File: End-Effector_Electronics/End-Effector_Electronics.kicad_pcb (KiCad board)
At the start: 2 copper layers, 65 x 57 mm, 34 parts, among them J1 Raspberry_Pi_2_3, J2 LynxServo, J3 LynxServo, J4 QWIIC_Generic_Conn, Q1 Q_PMOS_GSD, Q2 DMMT3906, Q3 Q_NMOS_GSD, U1 CAT24C32, U2 TDK_I3A4W008A033V, U3 LM22676MR-5

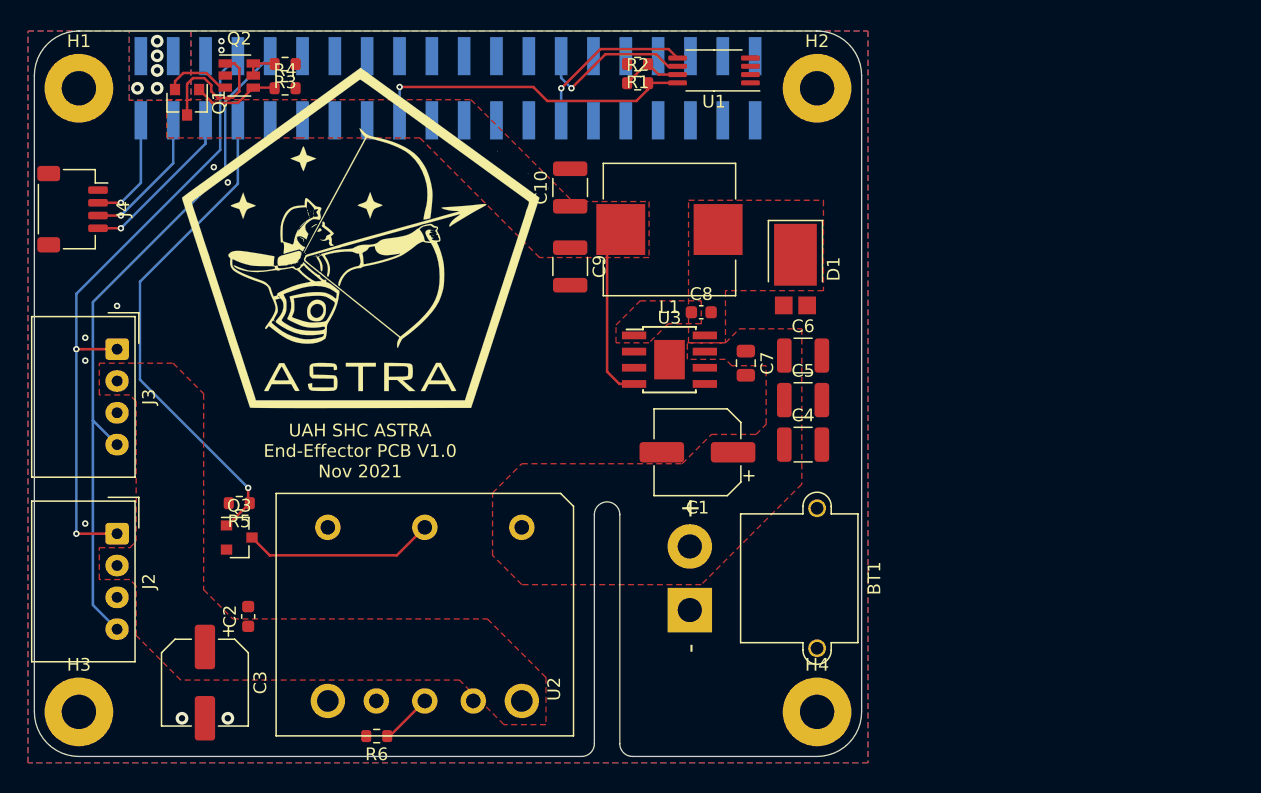
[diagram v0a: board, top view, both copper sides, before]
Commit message: added things and cleaned up silkscreen
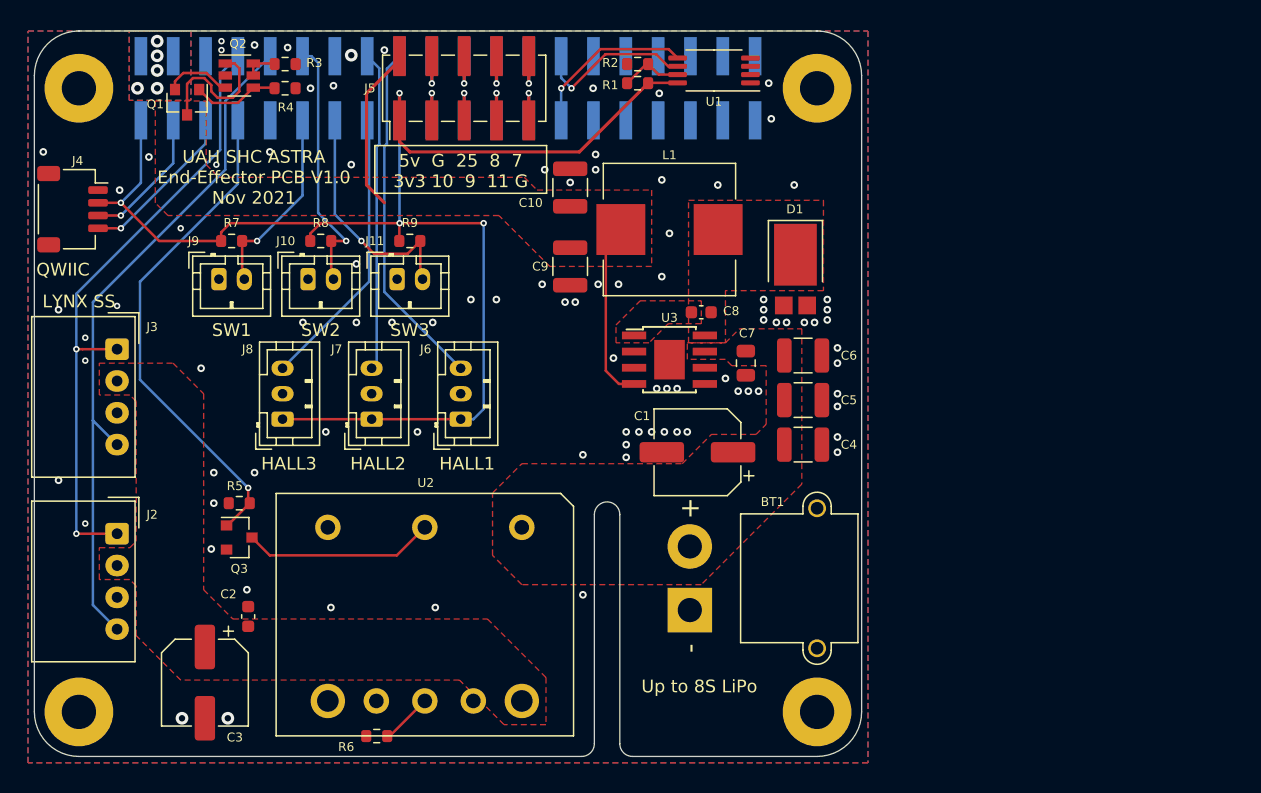
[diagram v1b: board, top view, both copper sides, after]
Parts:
- added J10: SW_Push_Open, Connector_JST:JST_PH_B2B-PH-K_1x02_P2.00mm_Vertical, F.Cu at (184.6, 97.5)
- added J11: SW_Push_Open, Connector_JST:JST_PH_B2B-PH-K_1x02_P2.00mm_Vertical, F.Cu at (191.6, 97.5)
- added J5: Conn_02x05_Odd_Even, Connector_PinHeader_2.54mm:PinHeader_2x05_P2.54mm_Vertical_SMD, F.Cu at (196.8, 82.5)
- added J6: AH1815-P-B, Connector_JST:JST_PH_B3B-PH-K_1x03_P2.00mm_Vertical, F.Cu at (196.6, 108.5)
- added J7: AH1815-P-B, Connector_JST:JST_PH_B3B-PH-K_1x03_P2.00mm_Vertical, F.Cu at (189.6, 108.5)
- added J8: AH1815-P-B, Connector_JST:JST_PH_B3B-PH-K_1x03_P2.00mm_Vertical, F.Cu at (182.6, 108.5)
- added J9: SW_Push_Open, Connector_JST:JST_PH_B2B-PH-K_1x02_P2.00mm_Vertical, F.Cu at (177.6, 97.5)
- added R7: 100k, Resistor_SMD:R_0603_1608Metric, F.Cu at (178.6, 94.5)
- added R8: 100k, Resistor_SMD:R_0603_1608Metric, F.Cu at (185.6, 94.5)
- added R9: 100k, Resistor_SMD:R_0603_1608Metric, F.Cu at (192.6, 94.5)
- G***: moved to B.Cu
- moved G*** 25.2 mm to (212.9, 101.0), turned to 180 degrees
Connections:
- H1 pad 1: (no net) -> Net-(H1-Pad1)
- H2 pad 1: (no net) -> Net-(H2-Pad1)
- H3 pad 1: (no net) -> Net-(H3-Pad1)
- H4 pad 1: (no net) -> Net-(H4-Pad1)
- J1 pad 11: (no net) -> /Limit_SW1
- J1 pad 12: (no net) -> /Limit_SW2
- J1 pad 13: (no net) -> /Limit_SW3
- J1 pad 15: (no net) -> /Hall3
- J1 pad 16: (no net) -> /Hall2
- J1 pad 18: (no net) -> /Hall1
- J1 pad 19: (no net) -> /GPIO10
- J1 pad 21: (no net) -> /GPIO9
- J1 pad 22: (no net) -> /GPIO25
- J1 pad 23: (no net) -> /GPIO11
- J1 pad 24: (no net) -> /GPIO8
- J1 pad 26: (no net) -> /GPIO7
- J1 pad 29: (no net) -> Net-(J1-Pad29)
- J1 pad 31: (no net) -> Net-(J1-Pad31)
- J1 pad 32: (no net) -> /GPIO12
- J1 pad 33: (no net) -> /GPIO13
- J1 pad 35: (no net) -> Net-(J1-Pad35)
- J1 pad 36: (no net) -> Net-(J1-Pad36)
- J1 pad 37: (no net) -> Net-(J1-Pad37)
- J1 pad 38: (no net) -> Net-(J1-Pad38)
- J1 pad 40: (no net) -> Net-(J1-Pad40)
- U2 pad 3: (no net) -> Net-(U2-Pad3)
- U2 pad 5: (no net) -> Net-(U2-Pad5)
- U2 pad 7: (no net) -> Net-(U2-Pad7)
- U3 pad 2: (no net) -> Net-(U3-Pad2)
- U3 pad 3: (no net) -> Net-(U3-Pad3)
- U3 pad 5: (no net) -> Net-(U3-Pad5)
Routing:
- net +3V3: track 34.7 -> 112.0 mm, vias 2 -> 4
- net /Hall1: track 0.00 -> 27.5 mm
- net /Hall2: track 0.00 -> 25.2 mm
- net /Hall3: track 0.00 -> 22.4 mm
- net /Limit_SW2: track 0.00 -> 20.6 mm, vias 0 -> 1
- net /Limit_SW3: track 0.00 -> 18.9 mm, vias 0 -> 1
- net /Limit_SW1: track 0.00 -> 15.2 mm, vias 0 -> 1
- net +5V: track 25.1 -> 38.4 mm
- net GND: track 0.00 -> 8.57 mm, vias 10 -> 94
- net /GPIO9: track 0.00 -> 4.28 mm, vias 0 -> 1
- net /GPIO11: track 0.00 -> 4.28 mm, vias 0 -> 1
- net /GPIO10: track 0.00 -> 4.28 mm, vias 0 -> 1
- net /GPIO8: track 0.00 -> 4.28 mm, vias 0 -> 1
- net /GPIO7: track 0.00 -> 4.28 mm, vias 0 -> 1
- net /GPIO25: track 0.00 -> 4.28 mm, vias 0 -> 1
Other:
- board text added: "5v G 25 8 7 3v3 10 9 11 G"
- board text added: "HALL1"
- board text added: "HALL2"
- board text added: "HALL3"
- board text added: "LYNX SS"
- board text added: "QWIIC"
- board text added: "SW1"
- board text added: "SW2"
- board text added: "SW3"
- board text added: "Up to 8S LiPo"

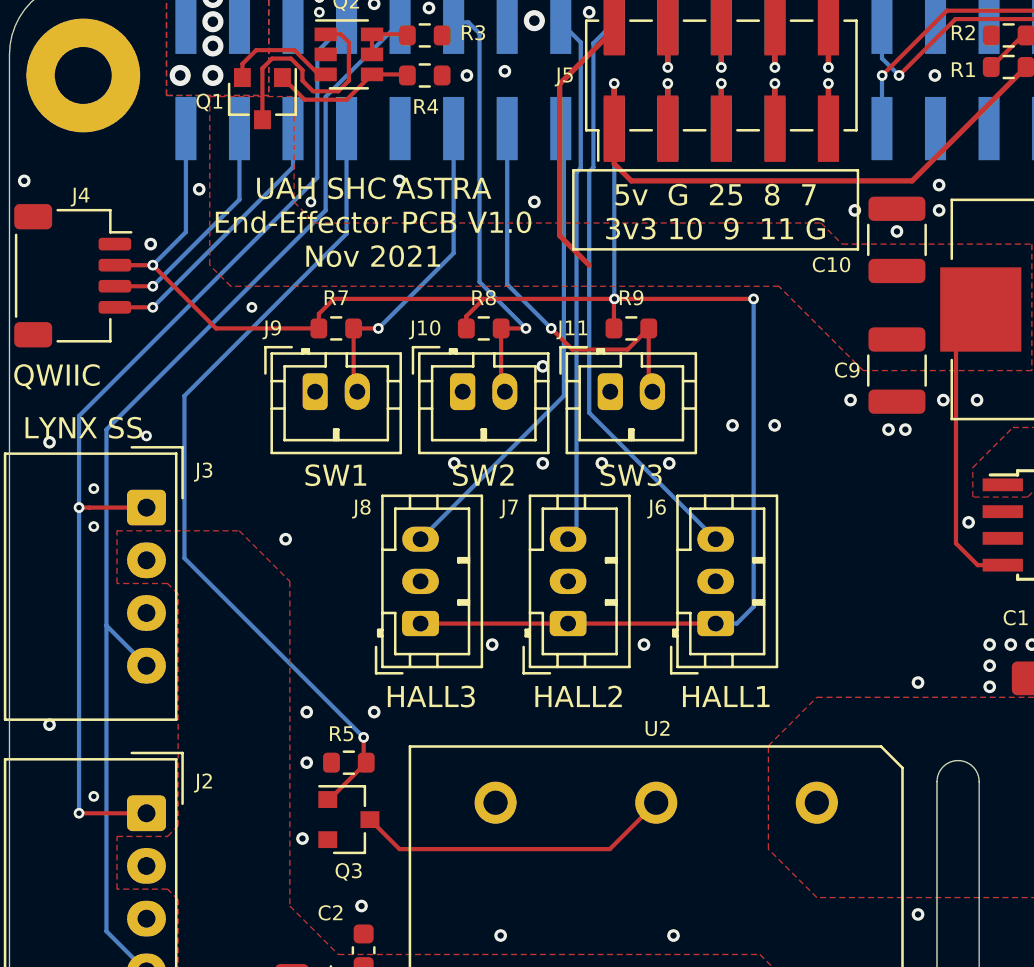
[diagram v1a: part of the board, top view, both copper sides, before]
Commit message: Swapped a few components
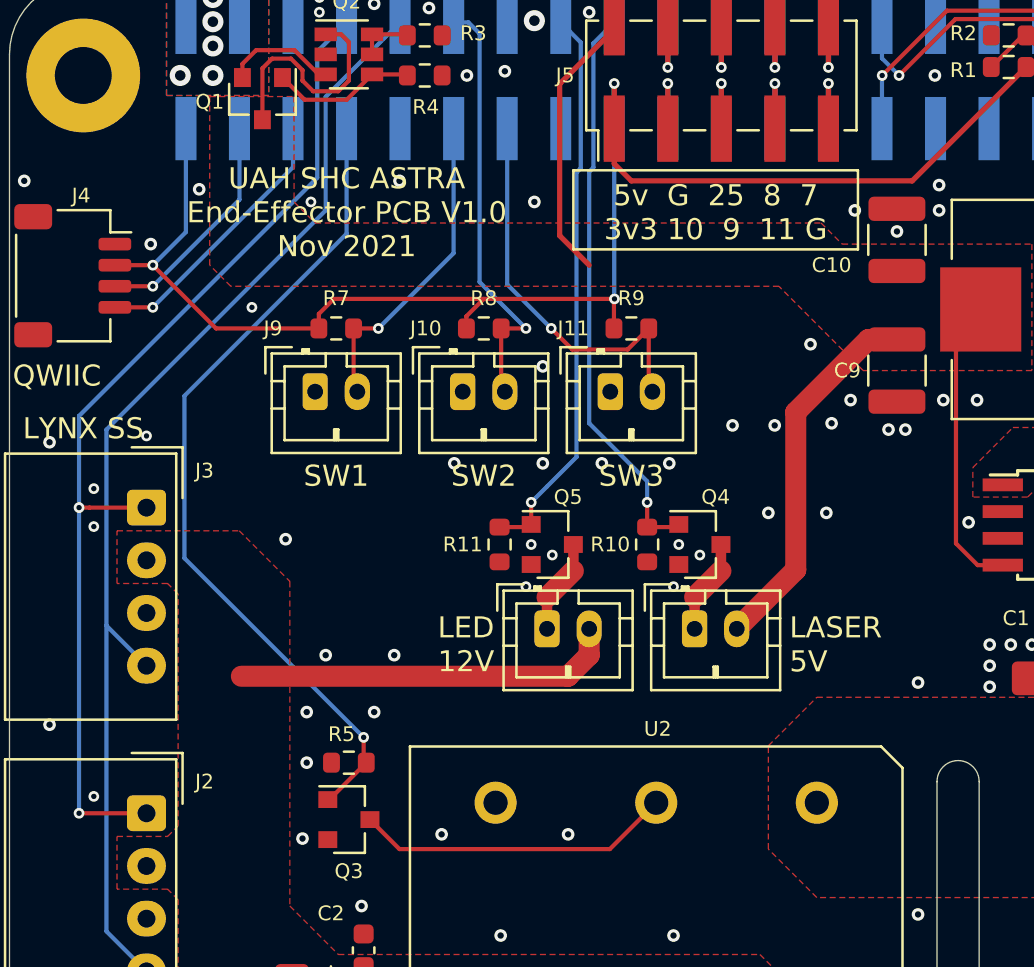
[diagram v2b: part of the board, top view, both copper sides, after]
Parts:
- removed J6, J7, J8: AH1815-P-B, Connector_JST:JST_PH_B3B-PH-K_1x03_P2.00mm_Vertical
- added D2: LED, Connector_JST:JST_PH_B2B-PH-K_1x02_P2.00mm_Vertical, F.Cu at (188.6, 108.8)
- added G***: LOGO, ASTRA_Footprints:SHCLogoSmall, B.Cu at (179.3, 109.0)
- added LD1: Laserdiode_1C2A, Connector_JST:JST_PH_B2B-PH-K_1x02_P2.00mm_Vertical, F.Cu at (195.6, 108.8)
- added Q4: Q_NMOS_GSD, Package_TO_SOT_SMD:SOT-23, F.Cu at (195.8, 104.8)
- added Q5: Q_NMOS_GSD, Package_TO_SOT_SMD:SOT-23, F.Cu at (188.8, 104.8)
- added R10: 100k, Resistor_SMD:R_0603_1608Metric, F.Cu at (193.3, 104.8)
- added R11: 100k, Resistor_SMD:R_0603_1608Metric, F.Cu at (186.3, 104.8)
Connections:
- J1 pad 15: /Hall3 -> Net-(J1-Pad15)
- J1 pad 16: /Hall2 -> /LED
- J1 pad 18: /Hall1 -> /Laser
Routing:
- net +3V3: track 112.0 -> 74.7 mm, vias 4 -> 3
- net /Hall1: track 27.5 -> 0.00 mm
- net /Laser: track 0.00 -> 27.1 mm, vias 0 -> 1
- net /LED: track 0.00 -> 26.7 mm, vias 0 -> 1
- net /Hall2: track 25.2 -> 0.00 mm
- net /Hall3: track 22.4 -> 0.00 mm
- net +12V: track 0.00 -> 18.2 mm
- net +5V: track 38.4 -> 56.0 mm
- net Net-(LD1-Pad1): track 0.00 -> 4.52 mm
- net Net-(D2-Pad1): track 0.00 -> 4.52 mm
- net GND: vias 94 -> 106
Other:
- board text added: "LASER 5V"
- board text added: "LED 12V"
- board text removed: "HALL1"
- board text removed: "HALL2"
- board text removed: "HALL3"

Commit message: tweaks
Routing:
- net GND: vias 106 -> 108
- net +BATT: vias 0 -> 8
- added copper zone on B.Cu, net +BATT
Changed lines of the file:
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@@
     (thickness 1.6)
     (drawings 28)
-    (tracks 304)
+    (tracks 314)
     (zones 0)
     (modules 48)
@@
   (gr_arc (start 166.58 131.55) (end 163.08 131.55) (angle -90) (layer Edge.Cuts) (width 0.05))
   (gr_arc (start 166.58 81.55) (end 166.58 78.05) (angle -90) (layer Edge.Cuts) (width 0.05))
+  (via (at 213.88 112.85) (size 0.6) (drill 0.3) (layers F.Cu B.Cu) (net 1))
+  (via (at 217.28 116.35) (size 0.6) (drill 0.3) (layers F.Cu B.Cu) (net 1))
+  (via (at 217.28 118.75) (size 0.6) (drill 0.3) (layers F.Cu B.Cu) (net 1))
+  (via (at 201.68 112.85) (size 0.6) (drill 0.3) (layers F.Cu B.Cu) (net 1))
+  (via (at 199.88 114.75) (size 0.6) (drill 0.3) (layers F.Cu B.Cu) (net 1))
+  (via (at 201.68 120.85) (size 0.6) (drill 0.3) (layers F.Cu B.Cu) (net 1))
+  (via (at 206.18 120.85) (size 0.6) (drill 0.3) (layers F.Cu B.Cu) (net 1))
+  (via (at 209.98 120.85) (size 0.6) (drill 0.3) (layers F.Cu B.Cu) (net 1))
   (via (at 178.28 132.05) (size 1) (drill 0.5) (layers F.Cu B.Cu) (net 2))
   (via (at 174.68 132.05) (size 1) (drill 0.5) (layers F.Cu B.Cu) (net 2))
@@
   (via (at 201.08 95.3) (size 0.6) (drill 0.3) (layers F.Cu B.Cu) (net 2))
   (via (at 202.08 99.05) (size 0.6) (drill 0.3) (layers F.Cu B.Cu) (net 2))
+  (via (at 213.08 101.65) (size 0.6) (drill 0.3) (layers F.Cu B.Cu) (net 2))
+  (via (at 213.88 101.65) (size 0.6) (drill 0.3) (layers F.Cu B.Cu) (net 2))
   (segment (start 189.58 111.05) (end 174.08 111.05) (width 1) (layer F.Cu) (net 3))
   (segment (start 190.58 110.05) (end 189.58 111.05) (width 1) (layer F.Cu) (net 3))
@@
       )
     )
+  )
+  (zone (net 1) (net_name +BATT) (layer B.Cu) (hatch edge 0.508)
+    (priority 9)
+    (connect_pads (clearance 0.2))
+    (min_thickness 0.2)
+    (fill yes (arc_segments 32) (thermal_gap 0.2) (thermal_bridge_width 1))
+    (polygon
+      (pts
+        (xy 215.48 121.55) (xy 201.38 121.55) (xy 199.08 119.25) (xy 199.08 114.35) (xy 201.38 112.05)
+        (xy 207.68 112.05) (xy 213.98 112.05) (xy 217.88 115.95) (xy 217.88 119.15)
+      )
+    )

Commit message: Fixed errors
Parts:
- BT1: footprint Connector_AMASS:AMASS_XT30PW-M_1x02_P2.50mm_Horizontal -> Connector_AMASS:AMASS_XT30U-M_1x02_P5.0mm_Vertical
- moved BT1 1.27 mm to (213.7, 124.5), turned to 90 degrees

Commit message: I changed something I guess?
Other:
- board text added: "M2.5 x4"

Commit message: Updated
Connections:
- U2 pad 3: Net-(U2-Pad3) -> GND
- U2 pad 7: Net-(U2-Pad7) -> +12V
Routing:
- net +12V: track 18.2 -> 22.0 mm
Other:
- board text added: "UAH SHC ASTRA End-Effector PCB V1.1 Mar 2022"
- board text removed: "UAH SHC ASTRA End-Effector PCB V1.0 Nov 2021"

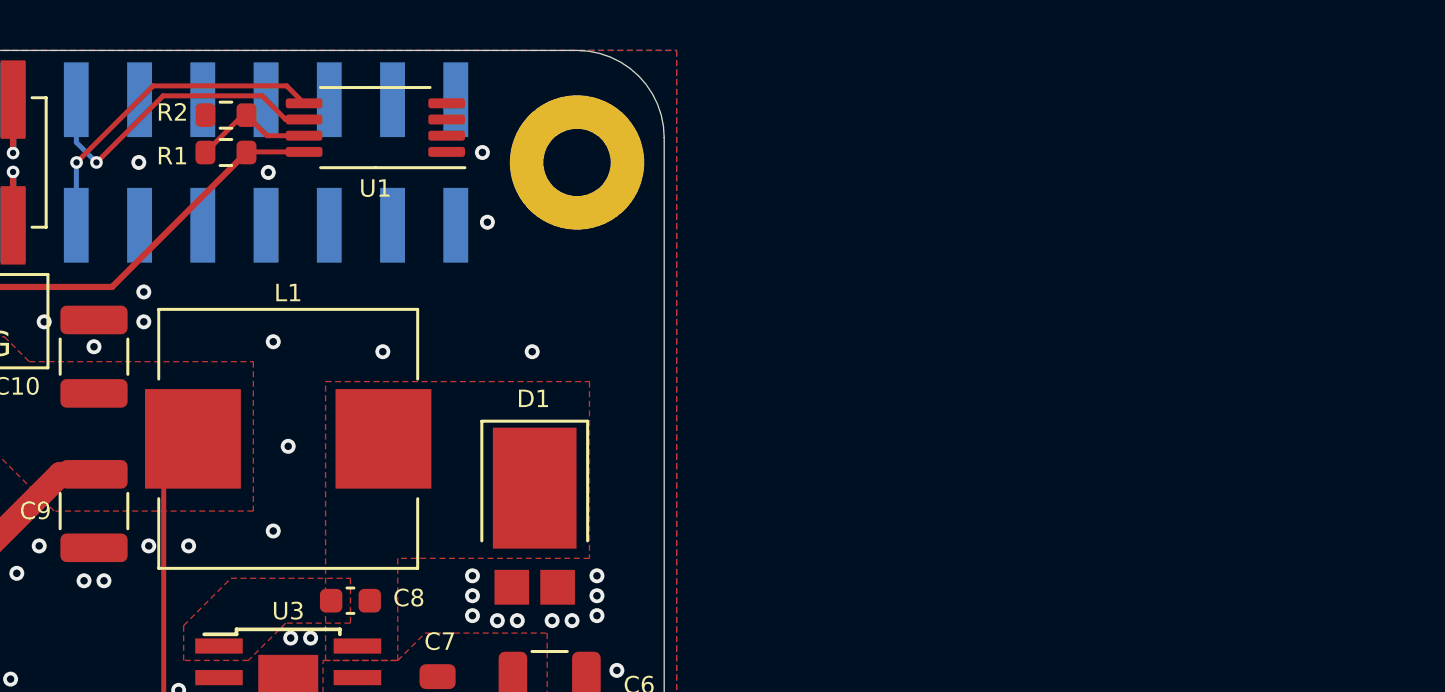
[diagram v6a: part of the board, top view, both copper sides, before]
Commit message: indicator LEDs
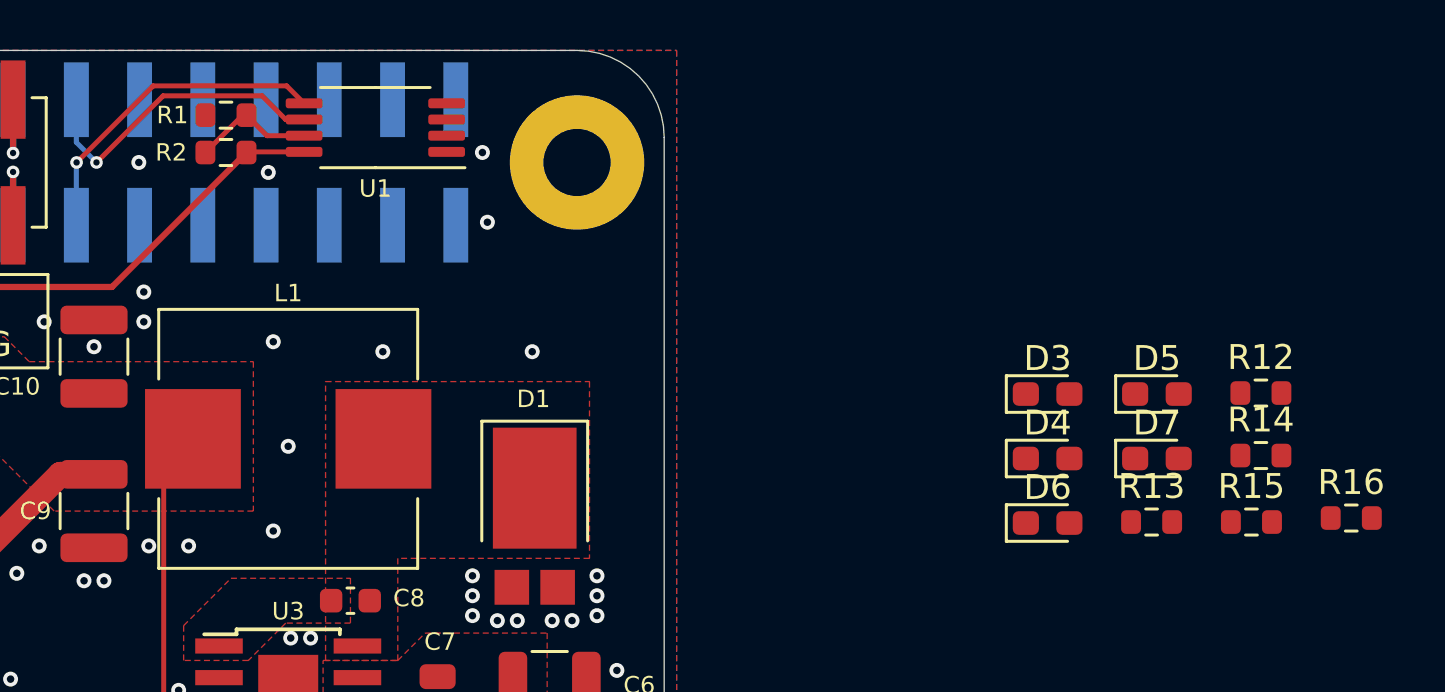
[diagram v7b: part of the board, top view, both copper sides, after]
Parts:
- added D3: G, LED_SMD:LED_0603_1608Metric_Pad1.05x0.95mm_HandSolder, F.Cu at (243.5, 91.8)
- added D4: G, LED_SMD:LED_0603_1608Metric_Pad1.05x0.95mm_HandSolder, F.Cu at (243.5, 94.4)
- added D5: G, LED_SMD:LED_0603_1608Metric_Pad1.05x0.95mm_HandSolder, F.Cu at (247.9, 91.8)
- added D6: G, LED_SMD:LED_0603_1608Metric_Pad1.05x0.95mm_HandSolder, F.Cu at (243.5, 97.0)
- added D7: G, LED_SMD:LED_0603_1608Metric_Pad1.05x0.95mm_HandSolder, F.Cu at (247.9, 94.4)
- added R12: 10, Resistor_SMD:R_0603_1608Metric, F.Cu at (252.0, 91.8)
- added R13: 180, Resistor_SMD:R_0603_1608Metric, F.Cu at (247.7, 97.0)
- added R14: 180, Resistor_SMD:R_0603_1608Metric, F.Cu at (252.0, 94.3)
- added R15: 1k, Resistor_SMD:R_0603_1608Metric, F.Cu at (251.7, 97.0)
- added R16: 3.3k, Resistor_SMD:R_0603_1608Metric, F.Cu at (255.7, 96.8)

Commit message: Indicator LEDs in PCB
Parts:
- moved R12 87.2 mm to (165.0, 86.8), turned to 180 degrees
- moved R14 80.1 mm to (172.0, 92.5), turned to 270 degrees
- moved D5 75.9 mm to (172.0, 89.2), turned to 90 degrees
- moved D3 75.5 mm to (168.2, 86.8)
- moved R13 74.0 mm to (173.8, 92.5), turned to 270 degrees
- moved R15 72.6 mm to (179.6, 105.3), turned to 90 degrees
- moved D4 69.9 mm to (173.8, 89.2), turned to 90 degrees
- moved D6 64.9 mm to (179.6, 108.5), turned to 270 degrees
- moved R16 36.6 mm to (225.5, 117.5)
- moved D7 34.4 mm to (222.3, 117.5), turned to 180 degrees
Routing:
- net /5V_RPI: track 5.49 -> 11.6 mm
- net +BATT: track 0.00 -> 4.58 mm
- net +3V3: track 74.7 -> 79.2 mm, vias 3 -> 4
- net +12V: track 22.0 -> 23.6 mm
- net Net-(D7-Pad1): track 0.00 -> 1.50 mm
- net Net-(D6-Pad1): track 0.00 -> 1.50 mm
- net Net-(D5-Pad1): track 0.00 -> 1.50 mm
- net Net-(D4-Pad1): track 0.00 -> 1.50 mm
- net Net-(D3-Pad1): track 0.00 -> 1.50 mm
- net GND: vias 108 -> 106
